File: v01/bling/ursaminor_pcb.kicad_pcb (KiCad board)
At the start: 2 copper layers, 298.8 x 122 mm, 229 parts, among them J1 USB_C_Receptacle_USB2.0, J2 I2C-L, J3 I2C-R, J4 AVR-ISP-6, SW1 Reset, U1 ATmega32U4-AU, U2 MCP23017_SO, U3 IS31FL3733-TQ, U4 HOLE, U4 IS31FL3733-TQ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

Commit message: Remove silkscreen from contacts and pad.
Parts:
- removed the REF** at (161.9, 123.0)
- removed the REF** at (190.2, 123.1)
- removed the REF** at (211.2, 37.9)
- removed the REF** at (140.7, 37.9)
- removed the REF** at (268.5, 118.8)
- removed the REF** at (83.8, 118.8)
- added REF**: MountingHole_2.2mm_M2_DIN965_Pad, MountingHole:MountingHole_2.2mm_M2_DIN965_Pad, F.Cu at (149.1, 110.3)
- added REF**: MountingHole_2.2mm_M2_DIN965_Pad, MountingHole:MountingHole_2.2mm_M2_DIN965_Pad, F.Cu at (177.5, 110.4)
- added REF**: MountingHole_2.2mm_M2_DIN965_Pad, MountingHole:MountingHole_2.2mm_M2_DIN965_Pad, F.Cu at (198.4, 25.1)
- added REF**: MountingHole_2.2mm_M2_DIN965_Pad, MountingHole:MountingHole_2.2mm_M2_DIN965_Pad, F.Cu at (128.0, 25.2)
- added REF**: MountingHole_2.2mm_M2_DIN965_Pad, MountingHole:MountingHole_2.2mm_M2_DIN965_Pad, F.Cu at (255.8, 106.1)
- added REF**: MountingHole_2.2mm_M2_DIN965_Pad, MountingHole:MountingHole_2.2mm_M2_DIN965_Pad, F.Cu at (71.0, 106.1)
- moved G*** 18.8 mm to (87.5, 74.9)
- moved G*** 18.1 mm to (238.6, 75.4)
- moved MX36 18.0 mm to (246.1, 44.2)
- moved MX30 18.0 mm to (246.1, 25.3)
- moved MX42 18.0 mm to (246.1, 63.2)
- moved D105 18.0 mm to (146.3, 121.3)
- moved D60 18.0 mm to (118.4, 32.4)
- moved MX27 18.0 mm to (146.3, 121.3)
- moved MX48 18.0 mm to (246.1, 82.3)
- moved D21 18.0 mm to (56.8, 78.7)
- moved D81 18.0 mm to (61.5, 68.1)
- moved D87 18.0 mm to (246.1, 63.3)
- moved C1 18.0 mm to (141.5, 77.4)
- moved C10 18.0 mm to (251.3, 107.0)
- moved C11 18.0 mm to (93.0, 108.8)
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
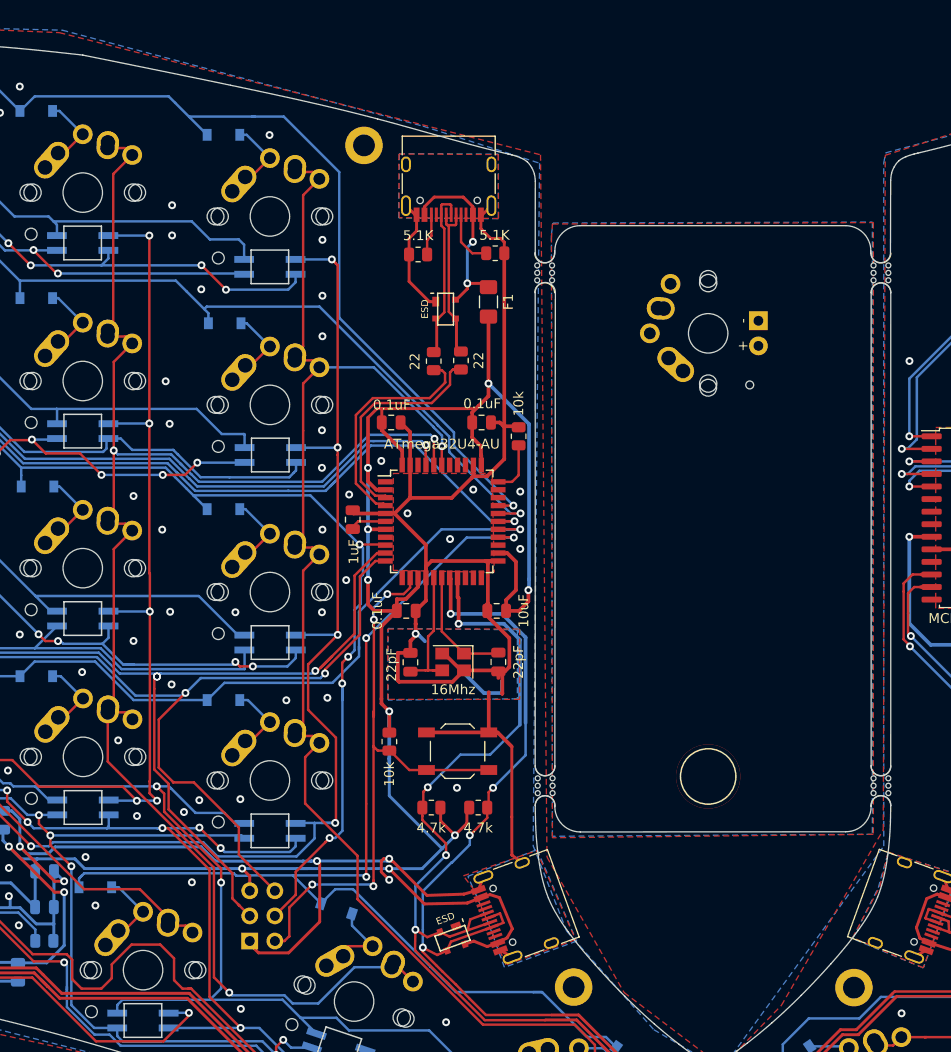
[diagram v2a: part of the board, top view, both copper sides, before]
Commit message: Use 5mm mousebites instead
The reveiwers at JLCPCB requested wider mousebites as 2mm
ones are 'too small'.
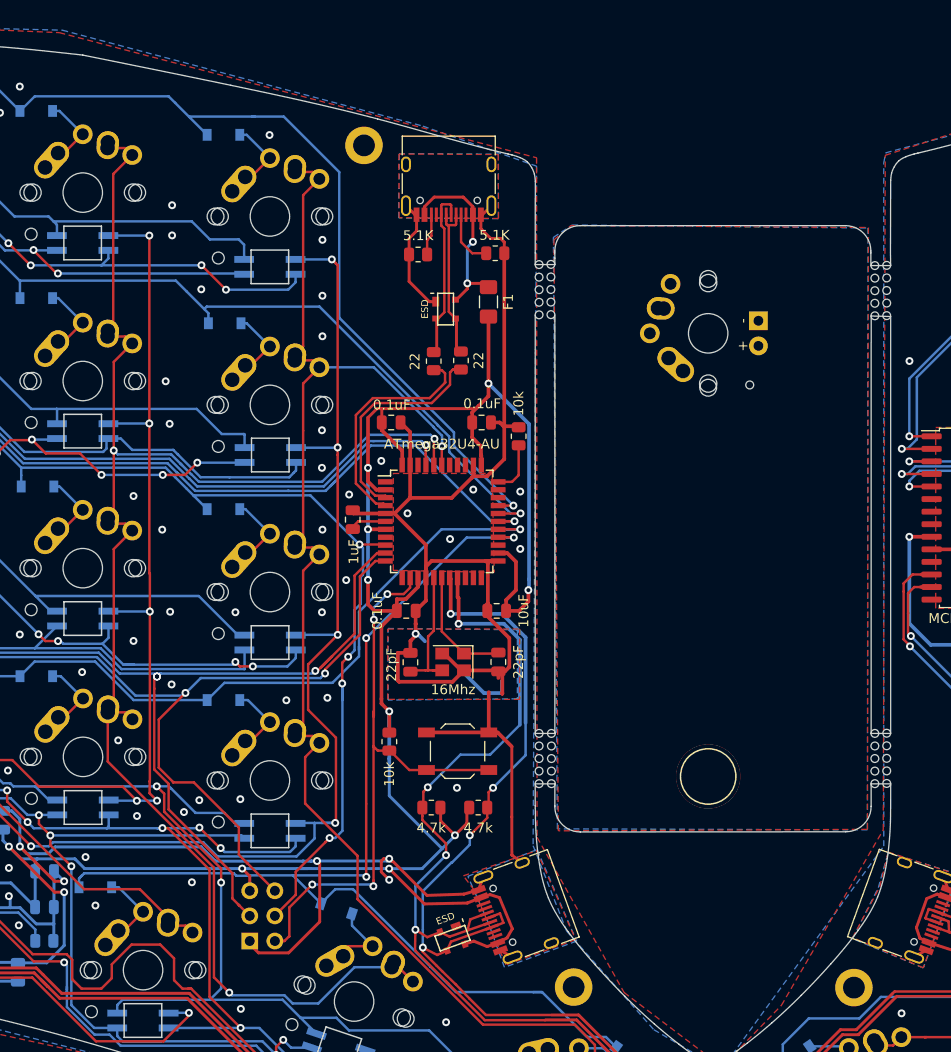
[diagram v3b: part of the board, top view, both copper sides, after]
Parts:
- removed mouse-bite-2mm-slot (x4): VAL**, Panelization:mouse-bite-2mm-slot
- added REF**: breakaway-mousebites, Keebio-Parts:breakaway-mousebites, F.Cu at (179.9, 87.2)
- added REF**: breakaway-mousebites, Keebio-Parts:breakaway-mousebites, F.Cu at (181.1, 87.2)
- added REF**: breakaway-mousebites, Keebio-Parts:breakaway-mousebites, F.Cu at (179.9, 39.9)
- added REF**: breakaway-mousebites, Keebio-Parts:breakaway-mousebites, F.Cu at (181.1, 39.9)
- added REF**: breakaway-mousebites, Keebio-Parts:breakaway-mousebites, F.Cu at (145.9, 39.8)
- added REF**: breakaway-mousebites, Keebio-Parts:breakaway-mousebites, F.Cu at (147.1, 39.8)
- added REF**: breakaway-mousebites, Keebio-Parts:breakaway-mousebites, F.Cu at (147.2, 87.2)
- added REF**: breakaway-mousebites, Keebio-Parts:breakaway-mousebites, F.Cu at (145.9, 87.2)
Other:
- outline, holes or cut-outs redrawn
